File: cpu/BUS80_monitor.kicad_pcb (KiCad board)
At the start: 2 copper layers, 12 parts

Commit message: Signed-off-by: Dmitry Ponyatov <dponyatov@gmail.com>
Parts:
- moved RX3 119.7 mm to (262.9, 83.8)
- moved RX4 96.7 mm to (262.9, 111.8)
- moved RX1 82.1 mm to (242.6, 83.8)
- moved RX2 80.2 mm to (242.6, 111.8)
- moved RX5 40.2 mm to (283.2, 83.8)
- moved HG1 37.0 mm to (242.6, 97.8)
- moved HG2 37.0 mm to (262.9, 97.8)
- moved HG3 37.0 mm to (283.2, 97.8)
- moved HG4 37.0 mm to (303.5, 97.8)
- moved RX7 37.0 mm to (303.5, 83.8)
- moved RX8 37.0 mm to (303.5, 111.8)
- moved RX6 17.8 mm to (283.2, 111.8)
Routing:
- net N-0000031: track 8.45 -> 0.00 mm
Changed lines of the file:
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@@
   (general
     (links 63)
-    (no_connects 62)
-    (area 172.72 46.99 353.06 214.63)
+    (no_connects 63)
+    (area 232.875445 80.451 315.289001 117.669)
     (thickness 1.6)
     (drawings 0)
-    (tracks 2)
+    (tracks 1)
     (zones 0)
     (modules 12)
@@
   (page A3)
   (layers
-    (15 F.Cu signal hide)
+    (15 F.Cu signal)
     (0 B.Cu signal)
     (16 B.Adhes user)
@@
   )
   (module R8_THRU (layer F.Cu)
-    (at 212.09 160.02)
+    (at 242.57 83.82)
     (fp_text reference RX1 (at 0 -2.54) (layer F.SilkS)
       (effects (font (size 1 1) (thickness 0.15)))
@@
   )
   (module R8_THRU (layer F.Cu)
-    (at 181.61 59.69)
+    (at 242.57 111.76)
     (fp_text reference RX2 (at 0 -2.54) (layer F.SilkS)
       (effects (font (size 1 1) (thickness 0.15)))
@@
   )
   (module R8_THRU (layer F.Cu)
-    (at 341.63 173.99)
+    (at 262.89 83.82)
     (fp_text reference RX3 (at 0 -2.54) (layer F.SilkS)
       (effects (font (size 1 1) (thickness 0.15)))
@@
   )
   (module R8_THRU (layer F.Cu)
-    (at 256.54 208.28)
+    (at 262.89 111.76)
     (fp_text reference RX4 (at 0 -2.54) (layer F.SilkS)
       (effects (font (size 1 1) (thickness 0.15)))
@@
   )
   (module R8_THRU (layer F.Cu)
-    (at 306.07 50.8)
+    (at 283.21 83.82)
     (fp_text reference RX5 (at 0 -2.54) (layer F.SilkS)
       (effects (font (size 1 1) (thickness 0.15)))
@@
   )
   (module R8_THRU (layer F.Cu)
-    (at 300.99 113.03)
+    (at 283.21 111.76)
     (fp_text reference RX6 (at 0 -2.54) (layer F.SilkS)
       (effects (font (size 1 1) (thickness 0.15)))
@@
   )
   (module R8_THRU (layer F.Cu)
-    (at 337.82 69.85)
+    (at 303.53 83.82)
     (fp_text reference RX7 (at 0 -2.54) (layer F.SilkS)
       (effects (font (size 1 1) (thickness 0.15)))
@@
   )
   (module R8_THRU (layer F.Cu)
-    (at 337.82 97.79)
+    (at 303.53 111.76)
     (fp_text reference RX8 (at 0 -2.54) (layer F.SilkS)
       (effects (font (size 1 1) (thickness 0.15)))
@@
   )
   (module DA04-11xWA (layer F.Cu)
-    (at 276.86 83.82)
+    (at 242.57 97.79)
     (fp_text reference HG1 (at -3.81 -2.54) (layer F.SilkS)
       (effects (font (size 1 1) (thickness 0.15)))
@@
   )
   (module DA04-11xWA (layer F.Cu)
-    (at 297.18 83.82)
+    (at 262.89 97.79)
     (fp_text reference HG2 (at -3.81 -2.54) (layer F.SilkS)
       (effects (font (size 1 1) (thickness 0.15)))
@@
   )
   (module DA04-11xWA (layer F.Cu)
-    (at 317.5 83.82)
+    (at 283.21 97.79)
     (fp_text reference HG3 (at -3.81 -2.54) (layer F.SilkS)
       (effects (font (size 1 1) (thickness 0.15)))
@@
   )
   (module DA04-11xWA (layer F.Cu)
-    (at 337.82 83.82)
+    (at 303.53 97.79)
     (fp_text reference HG4 (at -3.81 -2.54) (layer F.SilkS)
       (effects (font (size 1 1) (thickness 0.15)))
@@
     )
   )
-  (segment (start 347.98 78.74) (end 342.9 73.66) (width 0.254) (layer F.Cu) (net 20) (status 80000))
-  (segment (start 342.9 73.66) (end 342.9 72.39) (width 0.254) (layer F.Cu) (net 20) (status 80000))
+  (segment (start 308.61 86.36) (end 308.61 86.36) (width 0.5) (layer F.Cu) (net 20) (status 80030))
 )

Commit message: Signed-off-by: Dmitry Ponyatov <dponyatov@gmail.com>
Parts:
- removed RX7: R8, R8_THRU
- added R1: RR8, R8_THRU, F.Cu at (303.5, 83.8)
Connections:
- HG1 pad 10: N-0000076 (its old number) -> N-0000029
- HG1 pad 12: N-0000075 (its old number) -> N-0000030
- HG1 pad 14: N-0000079 -> N-0000026
- HG1 pad 16: N-0000078 (its old number) -> N-0000027
- HG1 pad 6: N-00000104 -> N-0000032
- HG1 pad 8: N-0000083 -> N-0000031
- HG3 pad 13: N-0000061 -> N-0000019
- HG4 pad 10: N-0000028 -> (no net)
- HG4 pad 11: N-0000023 (its old number) -> (no net)
- HG4 pad 12: N-0000027 -> (no net)
- HG4 pad 13: N-0000030 -> (no net)
- HG4 pad 14: N-0000034 -> (no net)
- HG4 pad 15: N-0000020 (its old number) -> (no net)
- HG4 pad 3: N-0000032 -> (no net)
- HG4 pad 6: N-0000025 (its old number) -> (no net)
- HG4 pad 7: N-0000024 (its old number) -> (no net)
- HG4 pad 8: N-0000026 -> (no net)
- HG4 pad 9: N-0000022 (its old number) -> (no net)
- RX1 pad 10: N-0000078 (its old number) -> N-0000027
- RX1 pad 11: N-0000079 -> N-0000026
- RX2 pad 1: N-0000076 (its old number) -> N-0000029
- RX2 pad 2: N-0000075 (its old number) -> N-0000030
- RX2 pad 3: N-0000083 -> N-0000031
- RX2 pad 4: N-00000104 -> N-0000032
- RX3 pad 9: N-0000093 -> (no net)
- RX4 pad 8: (no net) -> N-0000060
- RX5 pad 15: N-0000061 -> N-0000019
- RX5 pad 9: N-0000067 (its old number) -> (no net)
- RX6 pad 8: (no net) -> N-0000071
- RX8 pad 1: N-0000028 -> N-0000032
- RX8 pad 2: N-0000027 -> N-0000031
- RX8 pad 3: N-0000026 -> N-0000030
- RX8 pad 4: N-0000025 (its old number) -> N-0000029
- RX8 pad 5: N-0000024 (its old number) -> N-0000019
- RX8 pad 6: N-0000023 (its old number) -> N-0000027
- RX8 pad 7: N-0000022 (its old number) -> N-0000026
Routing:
- net /VCC5: track 0.00 -> 31.5 mm
- net N-0000067: track 0.00 -> 20.1 mm
- net N-0000070: track 0.00 -> 7.40 mm
- net N-0000078: track 0.00 -> 6.35 mm

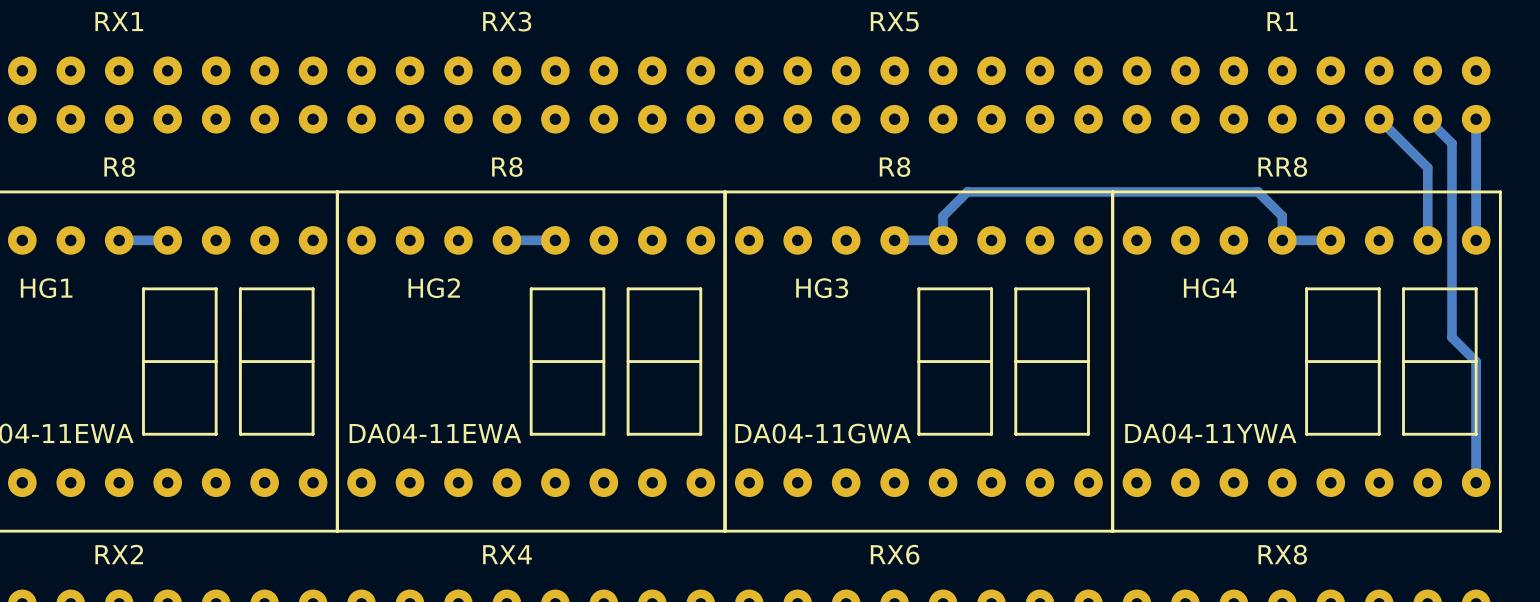
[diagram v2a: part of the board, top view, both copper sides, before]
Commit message: + NekroPower + lib/ LM7805 KR142EN5A  KR142EN12A
Signed-off-by: Dmitry Ponyatov <dponyatov@gmail.com>
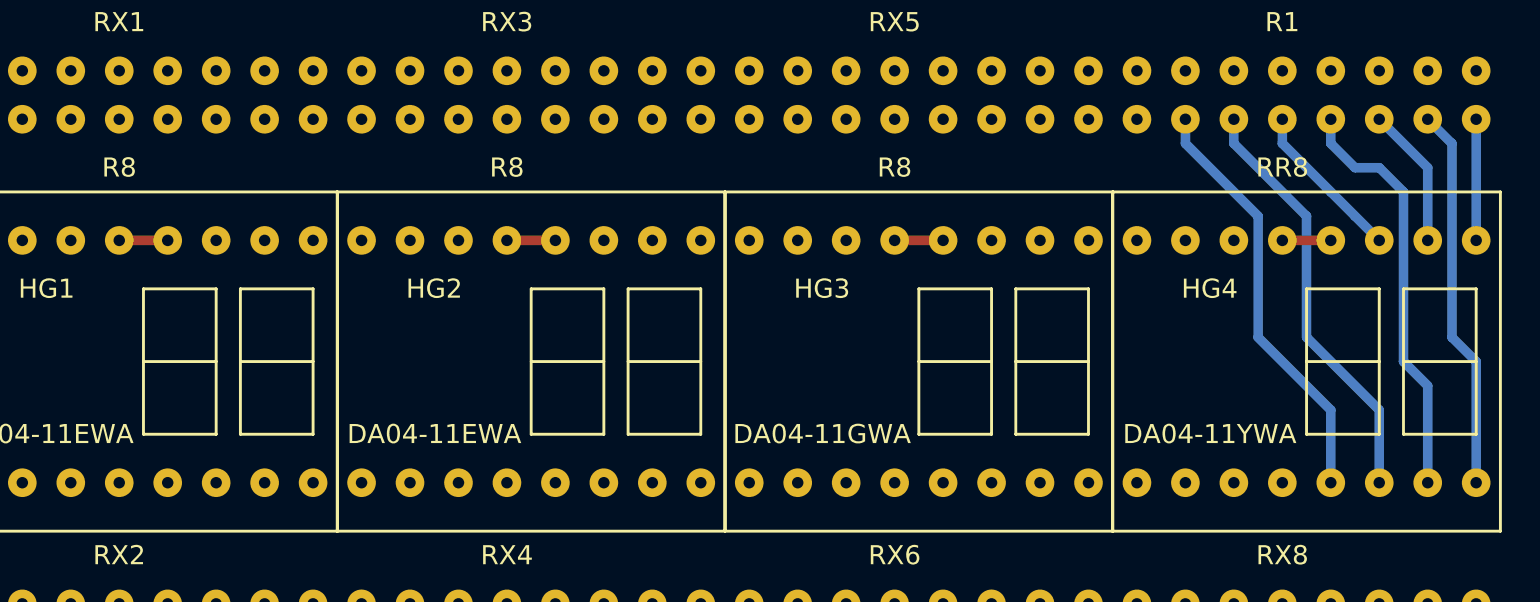
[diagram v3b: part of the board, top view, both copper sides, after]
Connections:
- net N-0000067 renamed /hg4g1
- net N-0000070 renamed /hg4e1
- net N-0000078 renamed /hg4c1
- HG1 pad 10: N-0000029 -> N-0000010
- HG1 pad 11: N-0000087 (its old number) -> N-0000030
- HG1 pad 12: N-0000030 -> N-0000034
- HG1 pad 14: N-0000026 -> N-000004
- HG1 pad 16: N-0000027 -> N-000003
- HG1 pad 7: N-0000049 -> N-0000031
- HG1 pad 8: N-0000031 -> N-0000033
- HG1 pad 9: N-0000088 -> N-0000029
- HG2 pad 10: N-0000053 -> N-0000019
- HG2 pad 13: N-0000051 -> N-0000026
- HG3 pad 13: N-0000019 -> N-0000011
- HG4 pad 13: (no net) -> /hg4b1
- HG4 pad 14: (no net) -> /hg4f1
- HG4 pad 15: (no net) -> /hg4a1
- HG4 pad 3: (no net) -> /hg4d1
- R1 pad 10: (no net) -> /hg4b1
- R1 pad 11: (no net) -> /hg4f1
- R1 pad 12: (no net) -> /hg4d1
- R1 pad 13: (no net) -> /hg4a1
- RX1 pad 10: N-0000027 -> N-000003
- RX1 pad 11: N-0000026 -> N-000004
- RX2 pad 1: N-0000029 -> N-0000010
- RX2 pad 2: N-0000030 -> N-0000034
- RX2 pad 3: N-0000031 -> N-0000033
- RX2 pad 5: N-0000049 -> N-0000031
- RX2 pad 6: N-0000087 (its old number) -> N-0000030
- RX2 pad 7: N-0000088 -> N-0000029
- RX3 pad 15: N-0000051 -> N-0000026
- RX4 pad 1: N-0000053 -> N-0000019
- RX5 pad 15: N-0000019 -> N-0000011
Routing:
- net /hg4f1: track 0.00 -> 22.2 mm
- net /hg4b1: track 0.00 -> 22.2 mm
- net /hg4a1: track 0.00 -> 21.9 mm
- net /VCC5: track 31.5 -> 10.2 mm
- net /hg4d1: track 0.00 -> 8.45 mm
